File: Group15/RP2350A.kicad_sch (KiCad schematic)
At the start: 3 parts, among them U1 RP2350A, U2 W25Q128JVS

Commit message: added board
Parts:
- added C2, C3: 15p, symbol Device:C
- added R1: 1k, symbol Device:R
- added Y1: ABM8-272-T3, Footprint_Library:XTAL_ABM8-272-T3, symbol Symbol_Library:ABM8-272-T3
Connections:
- net GND: now also C2.1, C3.1, Y1.2 (GND), Y1.4 (GND__1)
- net XIN: now reaches U1.21 (XIN)
- net XIN: now also C2.2, Y1.1
- net XOUT: now reaches U1.22 (XOUT)
- net XOUT: now also R1.1
- new net: C3.2, R1.2, Y1.3
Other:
- note added: "12MHz Crystal"
- moved on the sheet: U1

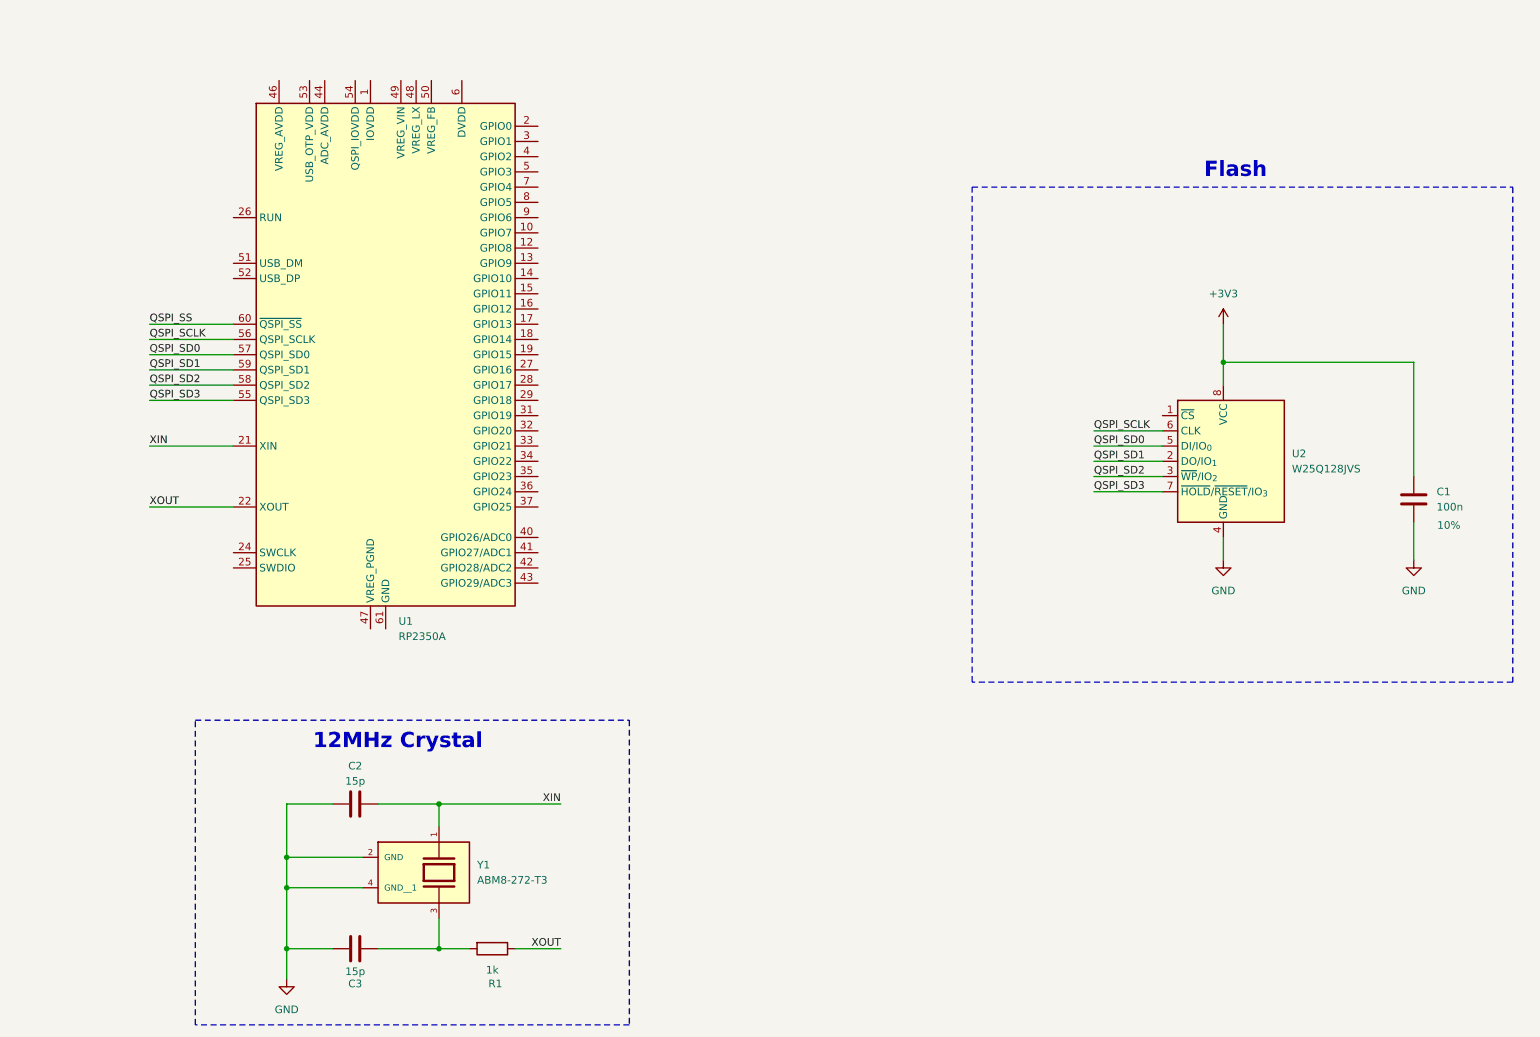
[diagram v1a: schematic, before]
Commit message: added Github Actions
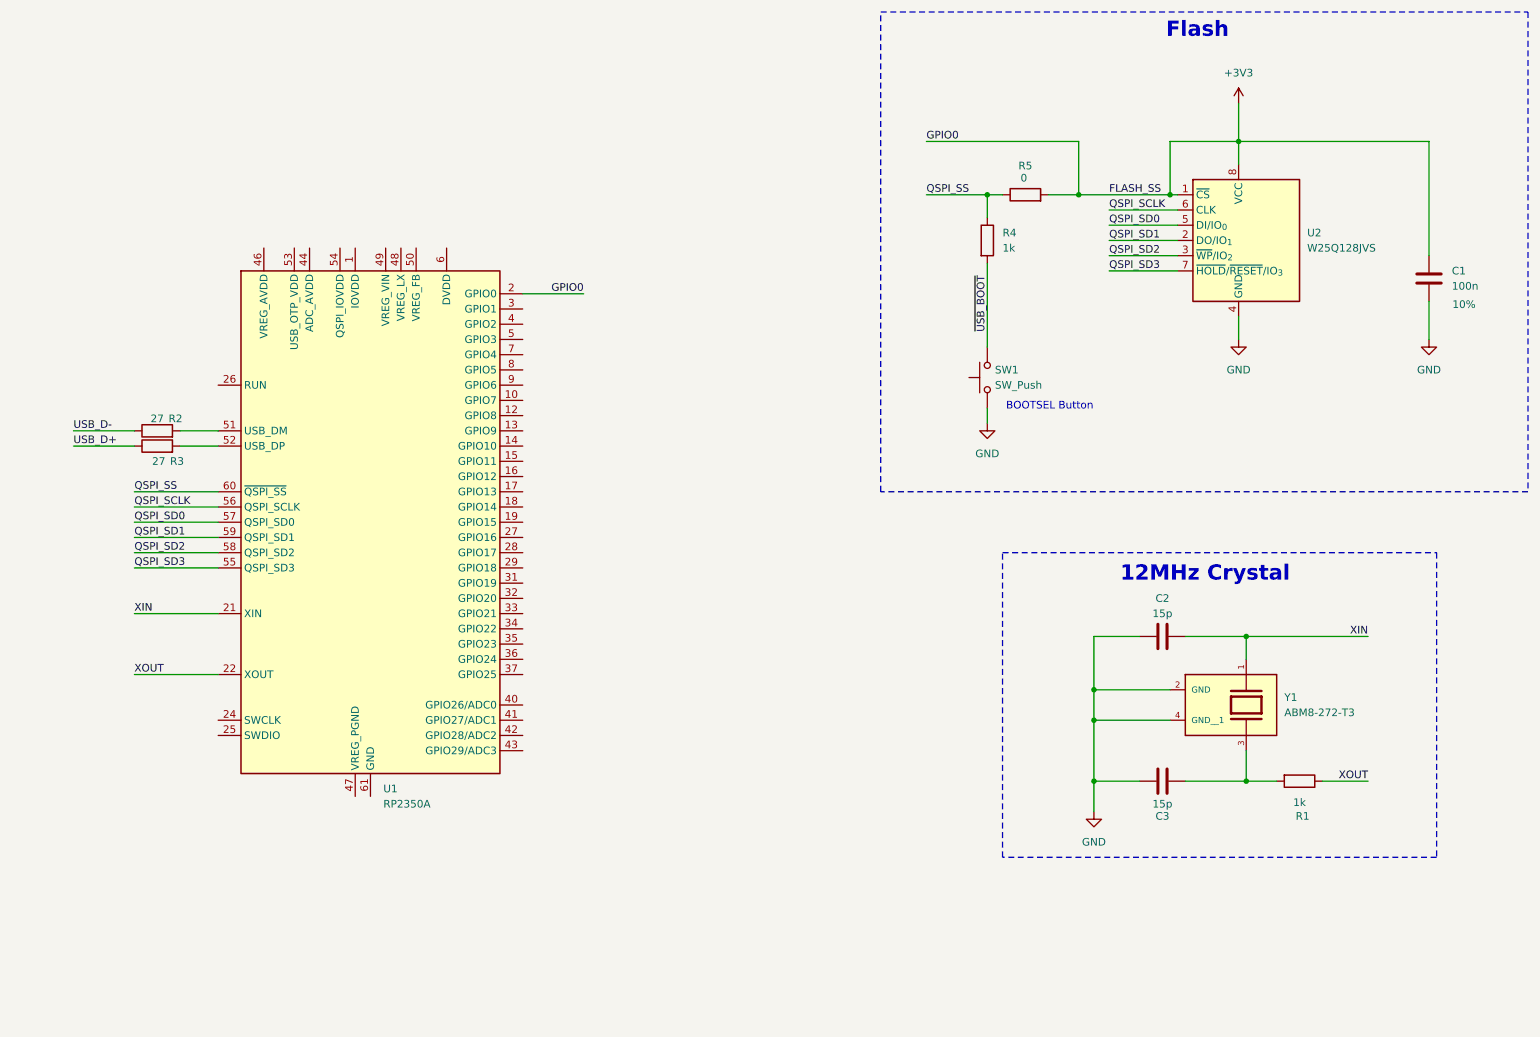
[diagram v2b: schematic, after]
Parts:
- added R2, R3: 27, symbol Device:R
- added R4: 1k, symbol Device:R
- added R5: 0, symbol Device:R
- added SW1: SW_Push, symbol Switch:SW_Push
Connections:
- net +3V3: now also U1.2 (GPIO0), U2.1 (~{CS}), R5.2
- net GND: now also SW1.1
- net QSPI_SS: now also R4.1, R5.1
- net at U1.51 (USB_DM): now also R2.2
- net at U1.52 (USB_DP): now also R3.2
- new net USB_D+: R3.1
- new net USB_D-: R2.1
- new net ~{USB_BOOT}: R4.2, SW1.2
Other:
- note added: "BOOTSEL Button"
- moved on the sheet: C1, C2, C3, R1, U1, U2, Y1

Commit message: added 5V buck
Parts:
- added U3: AP63205WU, Package_TO_SOT_SMD:TSOT-23-6, symbol Regulator_Switching:AP63205WU
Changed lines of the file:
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@@
+	)
+	(symbol
+		(lib_id "Regulator_Switching:AP63205WU")
+		(at 123.19 175.26 0)
+		(unit 1)
+		(body_style 1)
+		(exclude_from_sim no)
+		(in_bom yes)
+		(on_board yes)
+		(in_pos_files yes)
+		(dnp no)
+		(fields_autoplaced yes)
+		(property "Reference" "U3"
+			(at 123.19 165.1 0)
+			(show_name no)
+			(do_not_autoplace no)
+			(effects
+				(font
+					(size 1.27 1.27)
+				)
+			)
+		)
+		(property "Value" "AP63205WU"
+			(at 123.19 167.64 0)
+			(show_name no)
+			(do_not_autoplace no)
+			(effects
+				(font
+					(size 1.27 1.27)
+				)
+			)
+		)
+		(property "Footprint" "Package_TO_SOT_SMD:TSOT-23-6"
+			(at 123.19 198.12 0)
+			(hide yes)
+			(show_name no)
+			(do_not_autoplace no)
+			(effects
+				(font
+					(size 1.27 1.27)
+				)
+			)
+		)
+		(property "Datasheet" "https://www.diodes.com/assets/Datasheets/AP63200-AP63201-AP63203-AP63205.pdf"
+			(at 123.19 175.26 0)
+			(hide yes)
+			(show_name no)
+			(do_not_autoplace no)
+			(effects
+				(font
+					(size 1.27 1.27)
+				)
+			)
+		)
+		(property "Description" "2A, 1.1MHz Buck DC/DC Converter, fixed 5.0V output voltage, TSOT-23-6"
+			(at 123.19 175.26 0)
+			(hide yes)
+			(show_name no)
+			(do_not_autoplace no)
+			(effects
+				(font
+					(size 1.27 1.27)
+				)
+			)
+		)
+		(pin "5"
+		)
+		(pin "6"
+		)
+		(pin "3"
+		)
+		(pin "2"
+		)
+		(pin "4"
+		)
+		(pin "1"
+		)
+		(instances
+			(project "Group15"
+				(path "/d18e2577-1276-4c0d-bdfd-a503d70bff69/f3a1779e-924f-40b3-919f-c62ce97d678f"
+					(reference "U3")
+					(unit 1)
+				)
+			)
+		)
 	)
 	(symbol

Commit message: USB_C added
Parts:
- removed U3: AP63205WU, Package_TO_SOT_SMD:TSOT-23-6, symbol Regulator_Switching:AP63205WU
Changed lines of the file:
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@@
-		)
-	)
-	(label "USB_D+"
-		(at 27.94 90.17 0)
-		(effects
-			(font
-				(size 1.27 1.27)
-			)
-			(justify left bottom)
 		)
 	)
@@
 		)
 	)
-	(label "USB_D-"
-		(at 27.94 87.63 0)
-		(effects
-			(font
-				(size 1.27 1.27)
-			)
-			(justify left bottom)
-		)
-	)
 	(label "QSPI_SCLK"
 		(at 200.66 50.8 0)
@@
 			)
 			(justify right bottom)
+		)
+	)
+	(hierarchical_label "VBUS"
+		(shape input)
+		(at 82.55 43.18 0)
+		(effects
+			(font
+				(size 1.27 1.27)
+			)
+			(justify left)
+		)
+	)
+	(hierarchical_label "USB_D-"
+		(shape input)
+		(at 27.94 87.63 180)
+		(effects
+			(font
+				(size 1.27 1.27)
+			)
+			(justify right)
+		)
+	)
+	(hierarchical_label "USB_D+"
+		(shape input)
+		(at 27.94 90.17 180)
+		(effects
+			(font
+				(size 1.27 1.27)
+			)
+			(justify right)
 		)
 	)
@@
 					(unit 1)
 				)
-			)
-		)
-	)
-	(symbol
-		(lib_id "Regulator_Switching:AP63205WU")
-		(at 123.19 175.26 0)
-		(unit 1)
-		(body_style 1)
-		(exclude_from_sim no)
-		(in_bom yes)
-		(on_board yes)
-		(in_pos_files yes)
-		(dnp no)
-		(fields_autoplaced yes)
-		(property "Reference" "U3"
-			(at 123.19 165.1 0)
-			(show_name no)
-			(do_not_autoplace no)
-			(effects
-				(font
-					(size 1.27 1.27)
-				)
-			)
-		)
-		(property "Value" "AP63205WU"
-			(at 123.19 167.64 0)
-			(show_name no)
-			(do_not_autoplace no)
-			(effects
-				(font
-					(size 1.27 1.27)
-				)
-			)
-		)
-		(property "Footprint" "Package_TO_SOT_SMD:TSOT-23-6"
-			(at 123.19 198.12 0)
-			(hide yes)
-			(show_name no)
-			(do_not_autoplace no)
-			(effects
-				(font
-					(size 1.27 1.27)
-				)
-			)
-		)
-		(property "Datasheet" "https://www.diodes.com/assets/Datasheets/AP63200-AP63201-AP63203-AP63205.pdf"
-			(at 123.19 175.26 0)
-			(hide yes)
-			(show_name no)
-			(do_not_autoplace no)
-			(effects
-				(font
-					(size 1.27 1.27)
-				)
-			)
-		)
-		(property "Description" "2A, 1.1MHz Buck DC/DC Converter, fixed 5.0V output voltage, TSOT-23-6"
-			(at 123.19 175.26 0)
-			(hide yes)
-			(show_name no)
-			(do_not_autoplace no)
-			(effects
-				(font
-					(size 1.27 1.27)
-				)
-			)
-		)
-		(pin "5"
-		)
-		(pin "6"
-		)
-		(pin "3"
-		)
-		(pin "2"
-		)
-		(pin "4"
-		)
-		(pin "1"
-		)
-		(instances
-			(project "Group15"
-				(path "/d18e2577-1276-4c0d-bdfd-a503d70bff69/f3a1779e-924f-40b3-919f-c62ce97d678f"
-					(reference "U3")
-					(unit 1)
-				)

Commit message: changes in Temp
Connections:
- net GND: now also U1.47 (VREG_PGND), U1.61 (GND)
- net ADC1_uc: now reaches U1.41 (GPIO27/ADC1)
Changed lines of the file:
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@@
+	)
+	(junction
+		(at 76.2 148.59)
+		(diameter 0)
+		(color 0 0 0 0)
 	)
 	(junction
@@
 	(wire
 		(pts
+			(xy 76.2 148.59) (xy 77.47 148.59)
+		)
+		(stroke
+			(width 0)
+			(type default)
+		)
+	)
+	(wire
+		(pts
 			(xy 222.25 39.37) (xy 254 39.37)
 		)
@@
 	(wire
 		(pts
+			(xy 76.2 148.59) (xy 76.2 151.13)
+		)
+		(stroke
+			(width 0)
+			(type default)
+		)
+	)
+	(wire
+		(pts
+			(xy 74.93 148.59) (xy 76.2 148.59)
+		)
+		(stroke
+			(width 0)
+			(type default)
+		)
+	)
+	(wire
+		(pts
 			(xy 222.25 33.02) (xy 222.25 39.37)
 		)
@@
 		(pts
 			(xy 198.12 146.05) (xy 198.12 151.13)
+		)
+		(stroke
+			(width 0)
+			(type default)
+		)
+	)
+	(wire
+		(pts
+			(xy 102.87 135.89) (xy 109.22 135.89)
 		)
 		(stroke
@@
 			)
 			(justify right bottom)
+		)
+	)
+	(global_label "ADC1_uc"
+		(shape input)
+		(at 109.22 135.89 0)
+		(fields_autoplaced yes)
+		(effects
+			(font
+				(size 1.27 1.27)
+			)
+			(justify left)
+		)
+		(property "Intersheetrefs" "${INTERSHEET_REFS}"
+			(at 120.2485 135.89 0)
+			(hide yes)
+			(show_name no)
+			(do_not_autoplace no)
+			(effects
+				(font
+					(size 1.27 1.27)
+				)
+				(justify left)
+			)
 		)
 	)
@@
 					(unit 1)
 				)
+			)
+		)
+	)
+	(symbol
+		(lib_id "power:GND")
+		(at 76.2 151.13 0)
+		(unit 1)
+		(body_style 1)
+		(exclude_from_sim no)
+		(in_bom yes)
+		(on_board yes)
+		(in_pos_files yes)
+		(dnp no)
+		(fields_autoplaced yes)
+		(property "Reference" "#PWR025"
+			(at 76.2 157.48 0)
+			(hide yes)
+			(show_name no)
+			(do_not_autoplace no)
+			(effects
+				(font
+					(size 1.27 1.27)
+				)
+			)
+		)
+		(property "Value" "GND"
+			(at 76.2 156.21 0)
+			(show_name no)
+			(do_not_autoplace no)
+			(effects
+				(font
+					(size 1.27 1.27)
+				)
+			)
+		)
+		(property "Footprint" ""
+			(at 76.2 151.13 0)
+			(hide yes)
+			(show_name no)
+			(do_not_autoplace no)
+			(effects
+				(font
+					(size 1.27 1.27)
+				)
+			)
+		)
+		(property "Datasheet" ""
+			(at 76.2 151.13 0)
+			(hide yes)
+			(show_name no)
+			(do_not_autoplace no)
+			(effects
+				(font
+					(size 1.27 1.27)
+				)
+			)
+		)
+		(property "Description" "Power symbol creates a global label with name \"GND\" , ground"
+			(at 76.2 151.13 0)
+			(hide yes)
+			(show_name no)
+			(do_not_autoplace no)
+			(effects
+				(font
+					(size 1.27 1.27)
+				)
+			)
+		)
+		(pin "1"
+		)
+		(instances
+			(project "Group15"
+				(path "/d18e2577-1276-4c0d-bdfd-a503d70bff69/f3a1779e-924f-40b3-919f-c62ce97d678f"
+					(reference "#PWR025")
+					(unit 1)
+				)
